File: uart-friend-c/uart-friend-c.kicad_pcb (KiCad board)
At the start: 2 copper layers, 31.1 x 16.5 mm, 22 parts, among them P1 USB_OTG, P3 CONN_01X03, P4 CONN_01X03, P5 CONN_01X06, P6 CONN_01X03, Q1 Q_PMOS_GSD, U1 AP7365_ADJ_SOT-23-5, U2 CY7C65213-SSOP

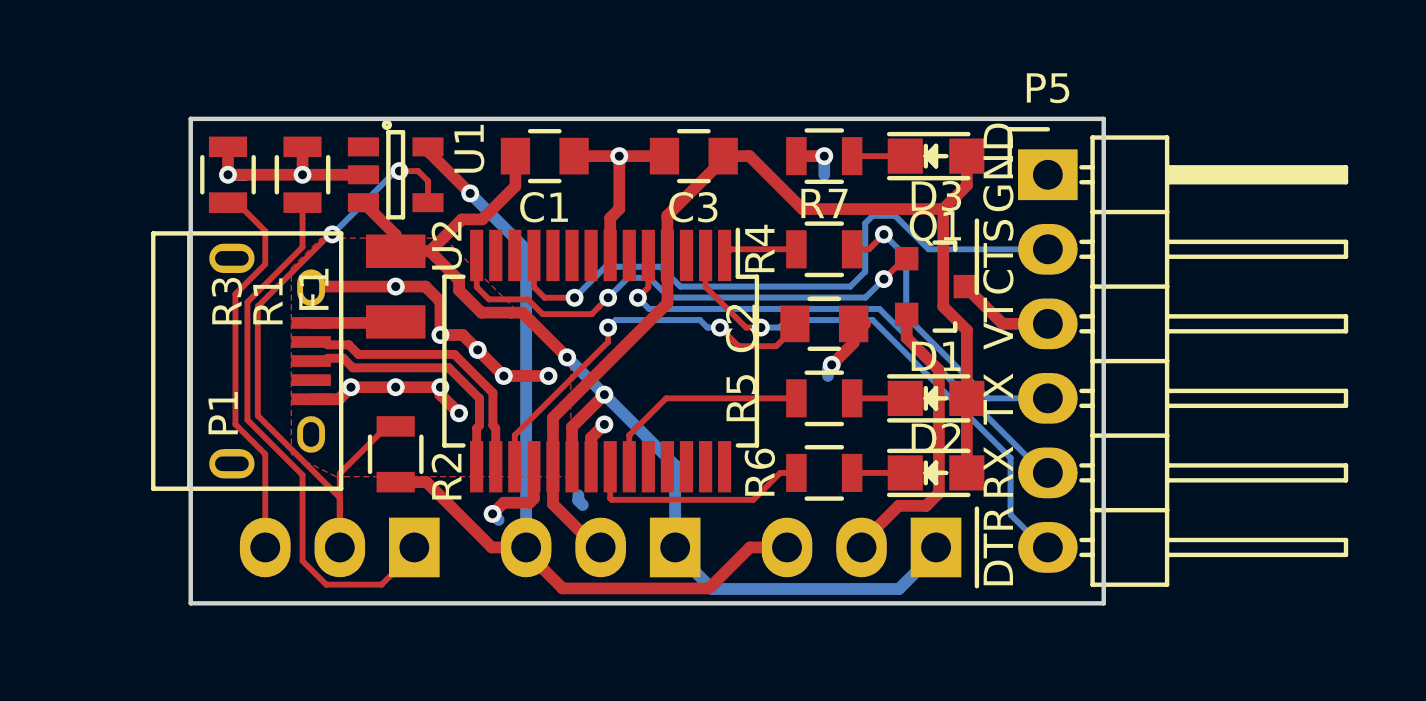
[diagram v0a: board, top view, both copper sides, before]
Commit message: add uart-friend-c R1 design
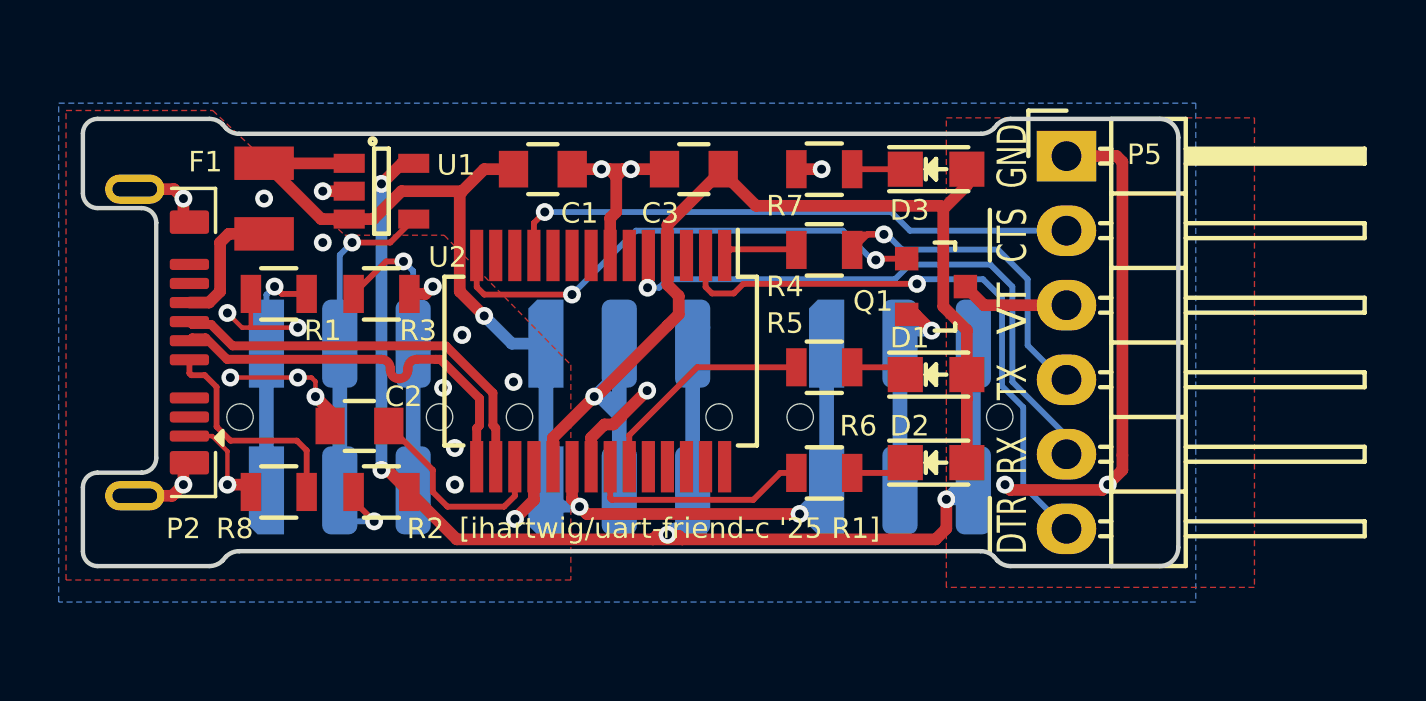
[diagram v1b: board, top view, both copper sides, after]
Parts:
- removed P1: USB_OTG, Connect:USB_Micro-B
- removed P3, P4, P6: CONN_01X03, Pin_Headers:Pin_Header_Angled_1x03
- added P2: USB_C_Plug_USB3.0_9P, uart-friend2-usb-special:USB_C_Plug_G-Switch_GT-USB-8016A_9P_TopMnt_Horizontal, F.Cu at (156.8, 97.2)
- added R8: 5.1k, Resistors_SMD:R_0805, F.Cu at (161.8, 102.2)
- added SW1: JS202011JAQN, uart-friend-special:Switch_SPDT_P2.5mm_RA_SMD_8x9mm, B.Cu at (163.8, 99.7)
- added SW2: JS202011JAQN, uart-friend-special:Switch_SPDT_P2.5mm_RA_SMD_8x9mm, B.Cu at (173.4, 99.7)
- added SW3: JS202011JAQN, uart-friend-special:Switch_SPDT_P2.5mm_RA_SMD_8x9mm, B.Cu at (182.9, 99.7)
- F1: value 500mA, 1206 -> 500mA-1206
- moved C2 16.2 mm to (164.5, 100.0), turned to 180 degrees
- moved R3 6.62 mm to (165.2, 95.5), turned to 0 degrees
- moved F1 5.40 mm to (161.2, 92.2)
- moved R1 4.14 mm to (161.8, 95.5), turned to 180 degrees
- moved R2 1.37 mm to (165.2, 102.2), turned to 180 degrees
- moved R5 1.06 mm to (180.3, 98.0)
- moved P5 0.90 mm to (188.6, 90.8)
- moved D1 0.81 mm to (184.2, 98.2)
- moved U1 0.74 mm to (165.2, 92.0)
- moved C1 0.45 mm to (170.8, 91.2)
- moved C3 0.44 mm to (175.9, 91.2)
- moved D3 0.44 mm to (184.2, 91.2)
- moved R7 0.44 mm to (180.3, 91.2)
- moved D2 0.35 mm to (184.2, 101.2)
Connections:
- net /~CTS renamed /~{CTS}
- net /~DTR renamed /~{DTR}
- net /~POWER renamed /~{POWER}
- net /~RXLED renamed /~{RXLED}
- net /~TXLED renamed /~{TXLED}
- U2 pad 10: (no net) -> unconnected-(U2-~{DCD}-Pad10)
- U2 pad 12: (no net) -> unconnected-(U2-GPIO4-Pad12)
- U2 pad 13: (no net) -> unconnected-(U2-GPIO2-Pad13)
- U2 pad 27: (no net) -> unconnected-(U2-GPIO6-Pad27)
- U2 pad 28: (no net) -> unconnected-(U2-GPIO7-Pad28)
- U2 pad 3: (no net) -> unconnected-(U2-~{RTS}-Pad3)
- U2 pad 6: (no net) -> unconnected-(U2-~{RI}-Pad6)
- U2 pad 8: (no net) -> unconnected-(U2-GPIO5-Pad8)
- U2 pad 9: (no net) -> unconnected-(U2-~{DSR}-Pad9)
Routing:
- net /FB_3V3: track 18.5 -> 3.26 mm, vias 0 -> 1
- net /FB_SEL: track 23.0 -> 9.75 mm
- net GND: track 38.3 -> 51.0 mm, vias 16 -> 24
- net /VREG: track 30.5 -> 40.6 mm, vias 1 -> 4
- net /FB_1V8: track 13.3 -> 5.10 mm, vias 0 -> 1
- net Net-(P2-CC): track 0.00 -> 7.75 mm
- net /VTARGET_Q: track 10.0 -> 2.34 mm, vias 0 -> 1
- net Net-(U2-VCCD): track 13.3 -> 7.02 mm, vias 2 -> 0
- net /USB_D+: track 8.71 -> 13.9 mm
- net /USB_D-: track 9.47 -> 13.9 mm
- net /~{DTR}: track 17.8 -> 20.6 mm
- net /RXD: track 18.0 -> 20.7 mm
- net +5V: track 35.7 -> 33.4 mm, vias 2 -> 3
- net /~{CTS}: track 21.9 -> 19.7 mm
- net /USB_VBUS: track 2.90 -> 4.49 mm
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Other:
- board size 31.1 x 16.5 mm -> 37.3 x 15.2 mm
- net class Default removed
- net class Power removed
- net class USB Signal removed
- rule pad_to_mask_clearance: 0.2 -> 0.05
- board text added: "[ihartwig/uart-friend-c '25 R1]"
- board text added: "~{CTS}"
- board text added: "~{DTR}"
- board text removed: "~CTS"
- board text removed: "~DTR"
